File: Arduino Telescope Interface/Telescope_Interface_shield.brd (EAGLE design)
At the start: 53.3 x 80 mm, 34 parts, among them IC1 40106N, IC2 24LC256P, J1 RJ45, J11 455-1750-1-ND, J12 455-1750-1-ND, J4 455-1750-1-ND, J8 455-1750-1-ND, J9 455-1750-1-ND, SW2 MOMENTARY-SWITCH-SPST-PTH-6.0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

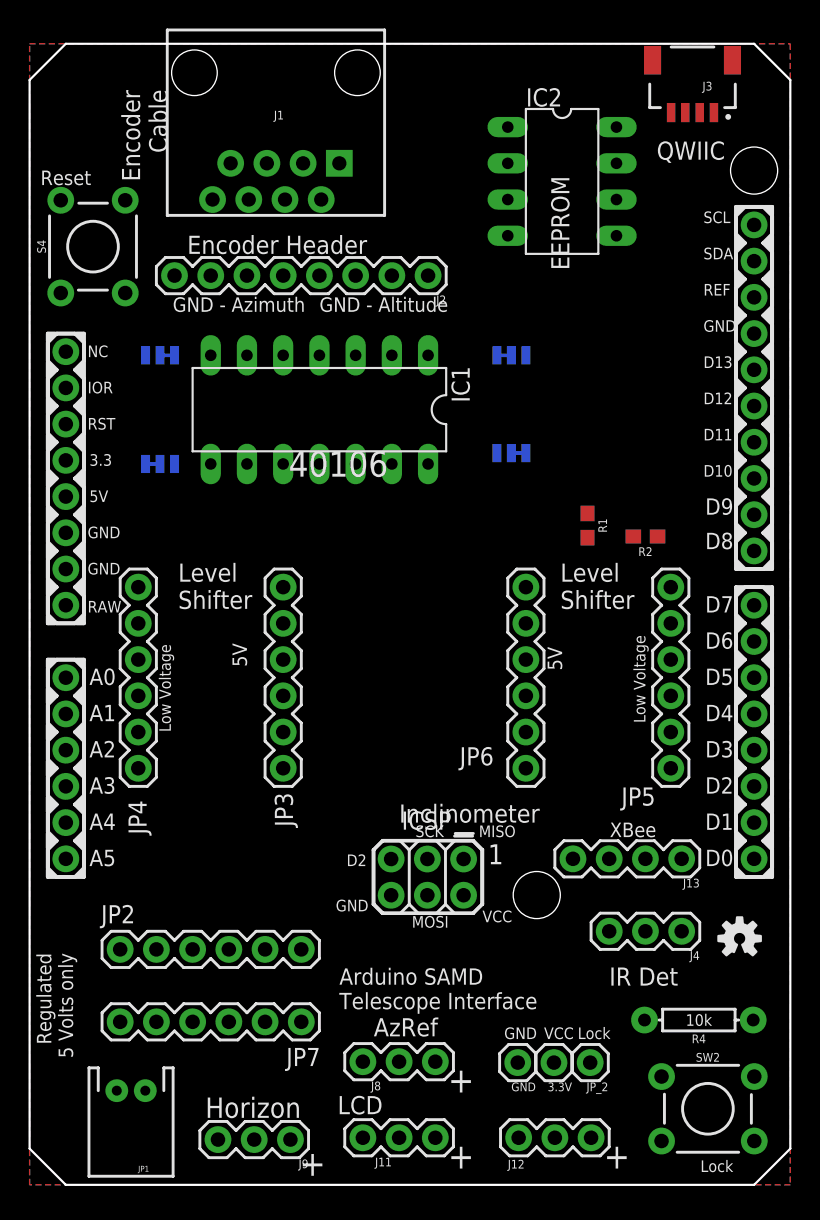
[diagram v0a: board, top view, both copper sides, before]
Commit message: Motor driver calls added
Motor driver calls added and Diagnostics sketch expanded for motor and OLED testing
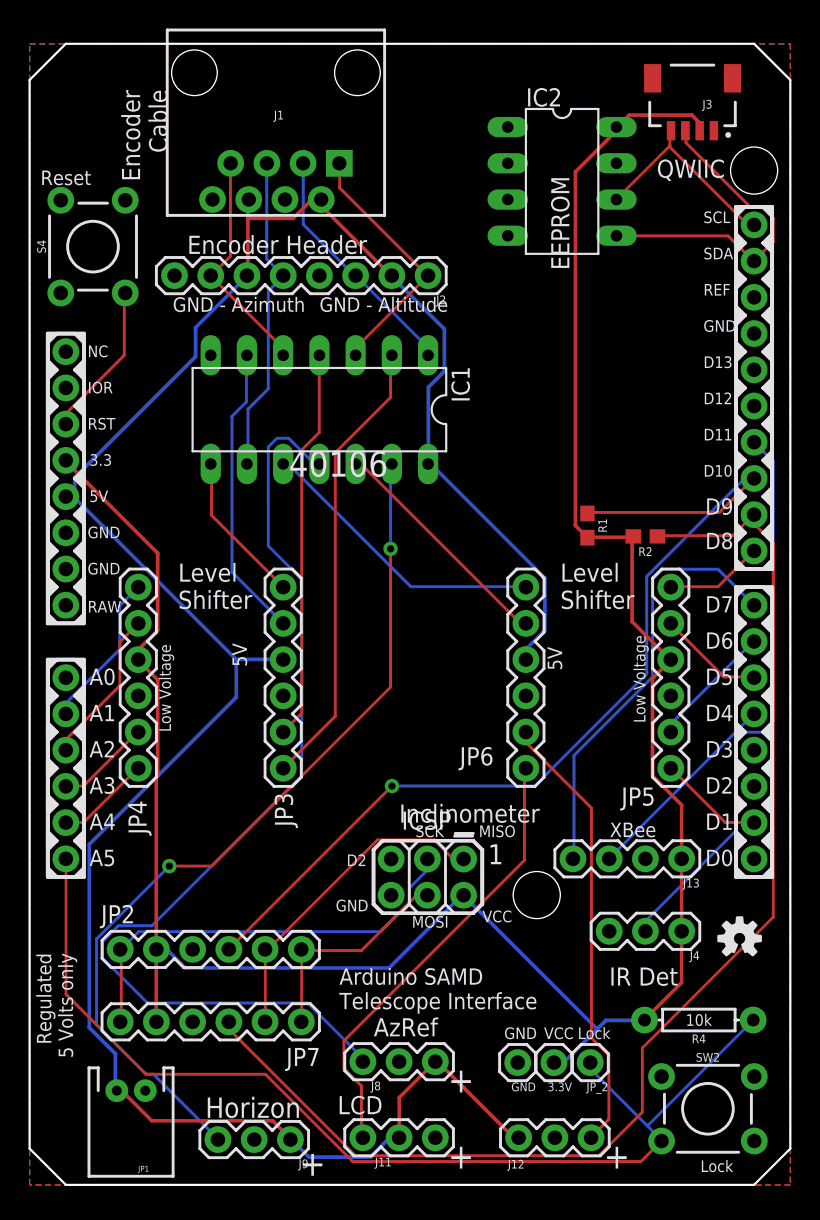
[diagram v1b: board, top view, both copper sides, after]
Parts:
- removed AL_A, AL_B, AZ_A, AZ_B: (no value), SparkFun-Jumpers:SMT-JUMPER_3_1-NC_TRACE_SILK
- moved J3 1.27 mm to (46.5, 73.9)
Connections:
- removed net N$1: AL_A.2, IC1.2
- removed net N$14: AZ_A.2, IC1.6
- removed net N$3: AL_B.2, IC1.4
- removed net N$4: AZ_B.2, IC1.8
- net AL_A: now also IC1.4; no longer AL_A.1, AL_B.3
- net AL_B: now also IC1.2; no longer AL_A.3, AL_B.1
- net AZ_A: now also IC1.6; no longer AZ_A.3, AZ_B.1
- net AZ_B: now also IC1.8; no longer AZ_A.1, AZ_B.3
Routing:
- net 3.3V: track 0.00 -> 166.3 mm
- net 5V: track 0.00 -> 164.8 mm
- net D9: track 0.00 -> 88.3 mm
- net A5: track 0.00 -> 74.8 mm
- net AZREF: track 0.00 -> 70.0 mm
- net D10: track 0.00 -> 67.2 mm, vias 0 -> 1
- net HORIZON: track 0.00 -> 61.5 mm, vias 0 -> 2
- net D11: track 0.00 -> 39.2 mm
- net AL_B: track 0.00 -> 32.1 mm
- net LCD: track 0.00 -> 31.8 mm
- net ZENITH: track 0.00 -> 31.4 mm
- net D7: track 0.00 -> 30.4 mm
- net SCK: track 0.00 -> 30.3 mm
- net AL_A: track 0.00 -> 27.5 mm
- net SDA: track 0.00 -> 23.1 mm
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
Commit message: Correction to interface shield
Correction to interface shield for Adafruit M4 Metro SAMD51 board that has 5V pin on ICSP connector
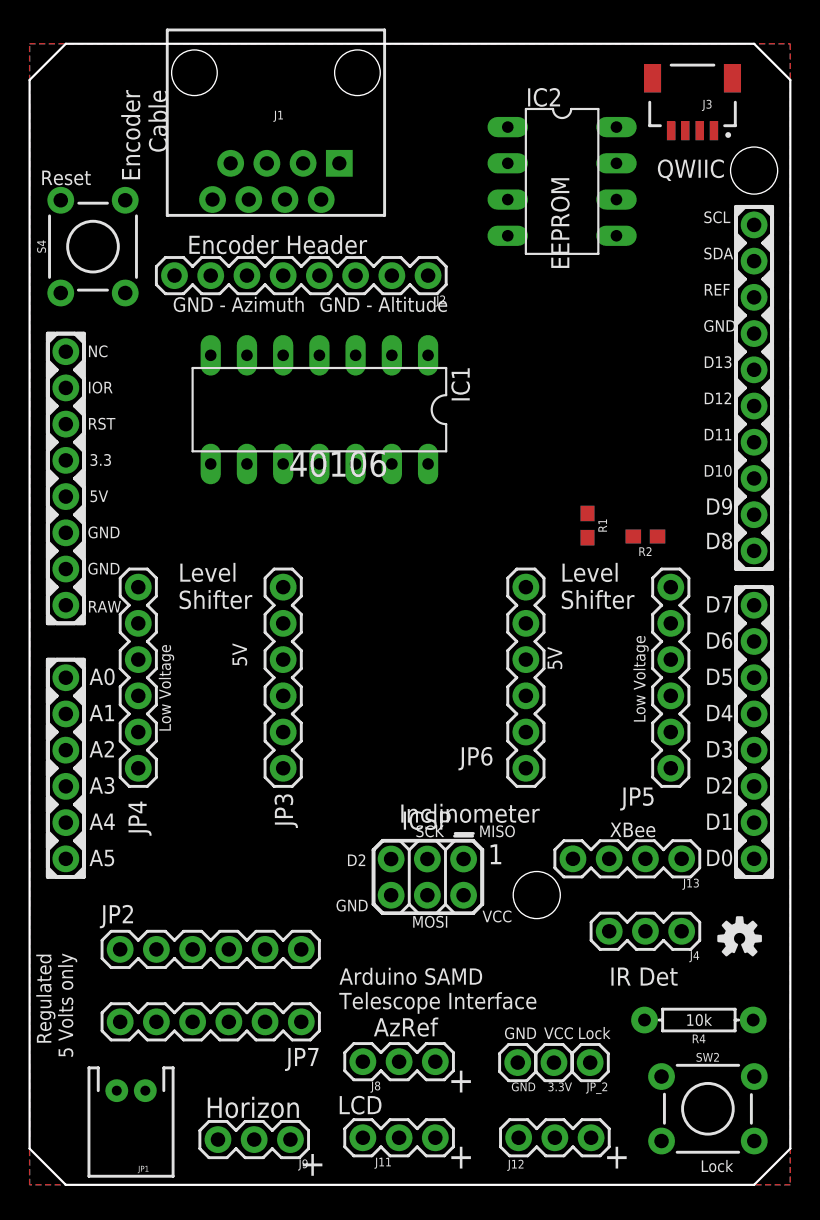
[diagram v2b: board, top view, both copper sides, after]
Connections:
- net 3.3V: no longer ICSP.2
- net 5V: now also ICSP.2
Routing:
- net 3.3V: track 166.3 -> 0.00 mm
- net 5V: track 164.8 -> 0.00 mm
- net D9: track 88.3 -> 0.00 mm
- net A5: track 74.8 -> 0.00 mm
- net AZREF: track 70.0 -> 0.00 mm
- net D10: track 67.2 -> 0.00 mm, vias 1 -> 0
- net HORIZON: track 61.5 -> 0.00 mm, vias 2 -> 0
- net D11: track 39.2 -> 0.00 mm
- net AL_B: track 32.1 -> 0.00 mm
- net LCD: track 31.8 -> 0.00 mm
- net ZENITH: track 31.4 -> 0.00 mm
- net D7: track 30.4 -> 0.00 mm
- net SCK: track 30.3 -> 0.00 mm
- net AL_A: track 27.5 -> 0.00 mm
- net SDA: track 23.1 -> 0.00 mm
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
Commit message: Update Eagle schematic files
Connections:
- net 3.3V: now also ICSP.2
- net 5V: no longer ICSP.2
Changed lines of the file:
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@@
 <autorouter>
 <pass name="Default">
-<param name="RoutingGrid" value="50mil"/>
+<param name="RoutingGrid" value="6.25mil"/>
 <param name="AutoGrid" value="1"/>
 <param name="Efforts" value="2"/>
 <param name="TopRouterVariant" value="1"/>
 <param name="tpViaShape" value="round"/>
-<param name="PrefDir.1" value="a"/>
+<param name="PrefDir.1" value="*"/>
 <param name="PrefDir.2" value="0"/>
 <param name="PrefDir.3" value="0"/>
@@
 <param name="PrefDir.14" value="0"/>
 <param name="PrefDir.15" value="0"/>
-<param name="PrefDir.16" value="a"/>
+<param name="PrefDir.16" value="-"/>
 <param name="cfVia" value="8"/>
 <param name="cfNonPref" value="5"/>
@@
 <contactref element="JP2" pad="3"/>
 <contactref element="J13" pad="2"/>
+<wire x1="33.528" y1="74.168" x2="47.982" y2="73.914" width="0" layer="19" extent="1-1"/>
+<wire x1="33.528" y1="71.628" x2="33.528" y2="74.168" width="0" layer="19" extent="1-1"/>
+<wire x1="33.528" y1="69.088" x2="33.528" y2="71.628" width="0" layer="19" extent="1-1"/>
+<wire x1="33.528" y1="66.548" x2="33.528" y2="69.088" width="0" layer="19" extent="1-1"/>
+<wire x1="20.32" y1="63.754" x2="33.528" y2="66.548" width="0" layer="19" extent="1-1"/>
+<wire x1="17.907" y1="69.088" x2="20.32" y2="63.754" width="0" layer="19" extent="1-1"/>
+<wire x1="12.827" y1="69.088" x2="17.907" y2="69.088" width="0" layer="19" extent="1-1"/>
+<wire x1="10.16" y1="63.754" x2="12.827" y2="69.088" width="0" layer="19" extent="1-1"/>
+<wire x1="12.7" y1="58.166" x2="10.16" y2="63.754" width="0" layer="19" extent="1-1"/>
+<wire x1="2.1844" y1="62.5348" x2="10.16" y2="63.754" width="0" layer="19" extent="1-1"/>
+<wire x1="50.8" y1="59.69" x2="47.982" y2="73.914" width="0" layer="19" extent="1-1"/>
+<wire x1="2.54" y1="45.72" x2="12.7" y2="58.166" width="0" layer="19" extent="1-1"/>
+<wire x1="2.54" y1="43.18" x2="2.54" y2="45.72" width="0" layer="19" extent="1-1"/>
+<wire x1="7.62" y1="34.29" x2="2.54" y2="43.18" width="0" layer="19" extent="1-1"/>
+<wire x1="17.78" y1="34.29" x2="7.62" y2="34.29" width="0" layer="19" extent="1-1"/>
+<wire x1="25.35" y1="20.307" x2="17.78" y2="34.29" width="0" layer="19" extent="1-1"/>
+<wire x1="25.908" y1="8.636" x2="25.35" y2="20.307" width="0" layer="19" extent="1-1"/>
+<wire x1="28.448" y1="3.302" x2="25.908" y2="8.636" width="0" layer="19" extent="1-1"/>
+<wire x1="34.2265" y1="8.5725" x2="28.448" y2="3.302" width="0" layer="19" extent="1-1"/>
+<wire x1="36.83" y1="3.302" x2="34.2265" y2="8.5725" width="0" layer="19" extent="1-1"/>
+<wire x1="44.3103" y1="7.5946" x2="36.83" y2="3.302" width="0" layer="19" extent="1-1"/>
+<wire x1="40.64" y1="17.78" x2="44.3103" y2="7.5946" width="0" layer="19" extent="1-1"/>
+<wire x1="43.18" y1="22.86" x2="40.64" y2="17.78" width="0" layer="19" extent="1-1"/>
+<wire x1="15.748" y1="3.175" x2="25.908" y2="8.636" width="0" layer="19" extent="1-1"/>
+<wire x1="8.112" y1="6.604" x2="15.748" y2="3.175" width="0" layer="19" extent="1-1"/>
+<wire x1="11.43" y1="11.43" x2="8.112" y2="6.604" width="0" layer="19" extent="1-1"/>
+<wire x1="11.43" y1="16.51" x2="11.43" y2="11.43" width="0" layer="19" extent="1-1"/>
+<wire x1="44.958" y1="34.29" x2="43.18" y2="22.86" width="0" layer="19" extent="1-1"/>
+<wire x1="34.798" y1="34.29" x2="44.958" y2="34.29" width="0" layer="19" extent="1-1"/>
 </signal>
 <signal name="RX">
@@
 <contactref element="J11" pad="2"/>
 <contactref element="J12" pad="1"/>
-<contactref element="ICSP" pad="2"/>
 <wire x1="15.367" y1="69.088" x2="20.447" y2="69.088" width="0" layer="19" extent="1-1"/>
 <wire x1="15.24" y1="63.754" x2="15.367" y2="69.088" width="0" layer="19" extent="1-1"/>
@@
 <wire x1="34.798" y1="36.83" x2="27.94" y2="50.546" width="0" layer="19" extent="1-1"/>
 <wire x1="17.78" y1="36.83" x2="34.798" y2="36.83" width="0" layer="19" extent="1-1"/>
-<wire x1="30.43" y1="20.307" x2="34.798" y2="36.83" width="0" layer="19" extent="1-1"/>
-<wire x1="28.448" y1="8.636" x2="30.43" y2="20.307" width="0" layer="19" extent="1-1"/>
+<wire x1="2.54" y1="48.26" x2="17.78" y2="36.83" width="0" layer="19" extent="1-1"/>
+<wire x1="28.448" y1="8.636" x2="34.798" y2="36.83" width="0" layer="19" extent="1-1"/>
 <wire x1="25.908" y1="3.302" x2="28.448" y2="8.636" width="0" layer="19" extent="1-1"/>
 <wire x1="18.288" y1="3.175" x2="25.908" y2="3.302" width="0" layer="19" extent="1-1"/>
 <wire x1="34.29" y1="3.302" x2="28.448" y2="8.636" width="0" layer="19" extent="1-1"/>
 <wire x1="6.112" y1="6.604" x2="18.288" y2="3.175" width="0" layer="19" extent="1-1"/>
-<wire x1="2.54" y1="48.26" x2="17.78" y2="36.83" width="0" layer="19" extent="1-1"/>
 </signal>
 <signal name="MOSI">
@@
 <contactref element="JP8" pad="3.3V"/>
 <contactref element="JP4" pad="4"/>
+<contactref element="ICSP" pad="2"/>
 <contactref element="J3" pad="2"/>
 <contactref element="J4" pad="1"/>
@@
 <wire x1="43.1165" y1="11.557" x2="45.72" y2="17.78" width="0" layer="19" extent="1-1"/>
 <wire x1="36.7665" y1="8.5725" x2="43.1165" y2="11.557" width="0" layer="19" extent="1-1"/>
-<wire x1="8.89" y1="11.43" x2="36.7665" y2="8.5725" width="0" layer="19" extent="1-1"/>
-<wire x1="8.89" y1="16.51" x2="8.89" y2="11.43" width="0" layer="19" extent="1-1"/>
+<wire x1="30.43" y1="20.307" x2="36.7665" y2="8.5725" width="0" layer="19" extent="1-1"/>
+<wire x1="8.89" y1="16.51" x2="30.43" y2="20.307" width="0" layer="19" extent="1-1"/>
+<wire x1="8.89" y1="11.43" x2="8.89" y2="16.51" width="0" layer="19" extent="1-1"/>
 <wire x1="7.62" y1="36.83" x2="8.89" y2="16.51" width="0" layer="19" extent="1-1"/>
 <wire x1="2.54" y1="50.8" x2="7.62" y2="36.83" width="0" layer="19" extent="1-1"/>
